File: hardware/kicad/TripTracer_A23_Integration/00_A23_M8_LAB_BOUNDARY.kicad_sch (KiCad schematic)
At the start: 4 parts, among them J901 BENCH ONLY VIN ON PIN1 / UNUS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, J902 M8 3pin VEHICLE (external)

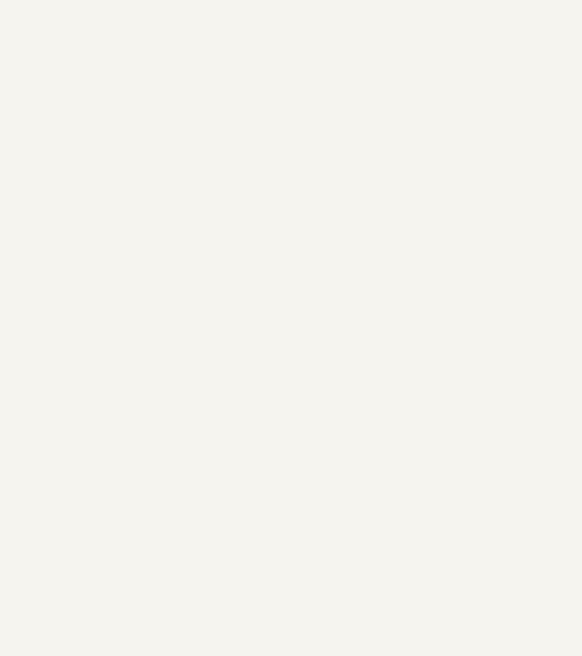
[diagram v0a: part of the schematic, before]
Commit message: TripPower A Round6: add real host HOLD and PWR_FAIL testpoints to isolated M8 lab page; NO FAB
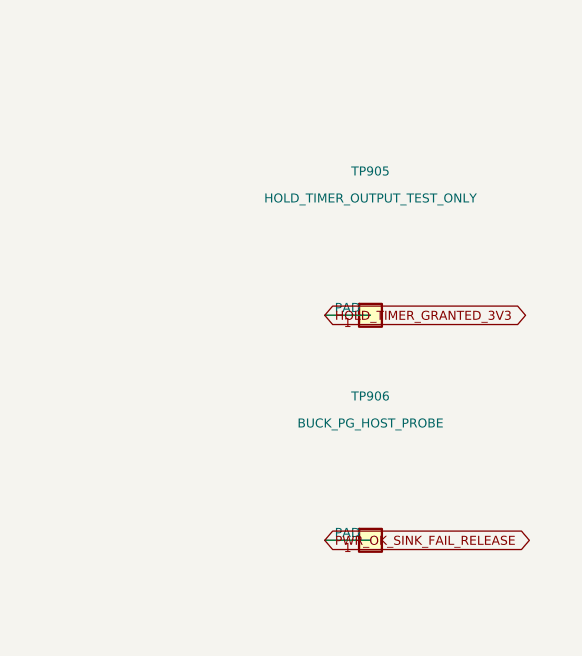
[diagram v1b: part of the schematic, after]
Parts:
- added TP905: HOLD_TIMER_OUTPUT_TEST_ONLY, TestPoint:TestPoint_Pad_1.5x1.5mm, symbol TripPower_PGOOD:SignalPad
- added TP906: BUCK_PG_HOST_PROBE, TestPoint:TestPoint_Pad_1.5x1.5mm, symbol TripPower_PGOOD:SignalPad
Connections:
- new net HOLD_TIMER_GRANTED_3V3: TP905.1 (PAD)
- new net PWR_OK_SINK_FAIL_RELEASE: TP906.1 (PAD)
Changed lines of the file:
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@@
 (wire (pts (xy 99.06 144.78) (xy 116.84 144.78)) (stroke (width 0) (type default)))
 (global_label "GND" (shape bidirectional) (at 116.84 144.78 0) (effects (font (size 1 1)) (justify left)))
+(symbol (lib_id "TripPower_PGOOD:SignalPad") (at 250 145 0) (unit 1) (in_bom no) (on_board yes) (dnp no)
+(property "Reference" "TP905" (at 250 129 0) (effects (font (size 1 1))))
+(property "Value" "HOLD_TIMER_OUTPUT_TEST_ONLY" (at 250 132 0) (effects (font (size 1 1))))
+(property "Footprint" "TestPoint:TestPoint_Pad_1.5x1.5mm" (at 250 145 0) (effects (font (size 1 1)) (hide yes)))
+(pin "1")
+(instances (project "TripTracer_A23_Integration" (path "/a26d9b0c-7f10-4e5a-a65f-000000000064/a26d9b0c-7f10-4e5a-a65f-000000000070" (reference "TP905") (unit 1)))))
+(wire (pts (xy 244.92 145) (xy 250 145)) (stroke (width 0) (type default)))
+(global_label "HOLD_TIMER_GRANTED_3V3" (shape bidirectional) (at 244.92 145 0) (effects (font (size 1 1)) (justify left)))
+(symbol (lib_id "TripPower_PGOOD:SignalPad") (at 250 170 0) (unit 1) (in_bom no) (on_board yes) (dnp no)
+(property "Reference" "TP906" (at 250 154 0) (effects (font (size 1 1))))
+(property "Value" "BUCK_PG_HOST_PROBE" (at 250 157 0) (effects (font (size 1 1))))
+(property "Footprint" "TestPoint:TestPoint_Pad_1.5x1.5mm" (at 250 170 0) (effects (font (size 1 1)) (hide yes)))
+(pin "1")
+(instances (project "TripTracer_A23_Integration" (path "/a26d9b0c-7f10-4e5a-a65f-000000000064/a26d9b0c-7f10-4e5a-a65f-000000000070" (reference "TP906") (unit 1)))))
+(wire (pts (xy 244.92 170) (xy 250 170)) (stroke (width 0) (type default)))
+(global_label "PWR_OK_SINK_FAIL_RELEASE" (shape bidirectional) (at 244.92 170 0) (effects (font (size 1 1)) (justify left)))
 (embedded_fonts no)
 )
